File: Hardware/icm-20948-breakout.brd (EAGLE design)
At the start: 19.3 x 10.5 mm, 11 parts, among them J1 455-1750-1-ND, J2 455-1750-1-ND, U1 NCP563, U2 NTS0104, U3 ICM-20948

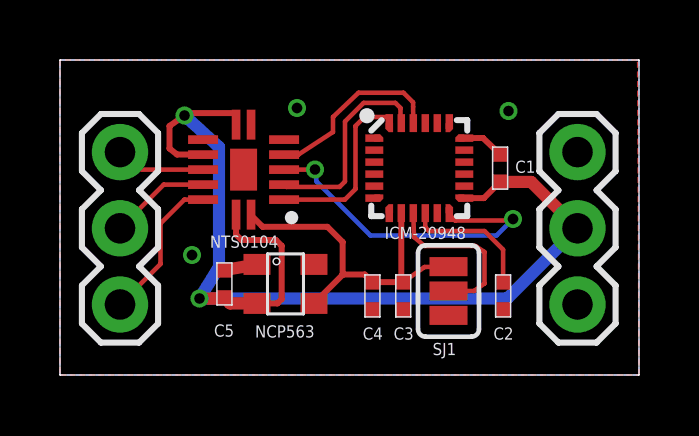
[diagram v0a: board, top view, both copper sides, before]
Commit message: Updated ICM footprint. The design rules of OSH Park are now met.
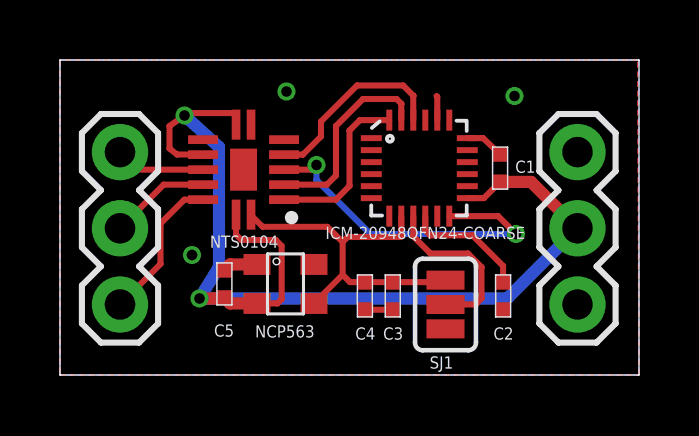
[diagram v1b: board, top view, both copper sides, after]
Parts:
- U3: value ICM-20948 -> ICM-20948QFN24-COARSE; device david-mems:QFN24-3X3 -> david-mems:SPARKFUN-SENSORS_MPU-9250
- moved SJ1 0.46 mm to (12.8, 2.35)
- moved C3 0.35 mm to (11.1, 2.64)
- moved C4 0.25 mm to (10.2, 2.64)
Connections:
- net GND: now also U3.20
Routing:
- net GND: track 2.59 -> 4.35 mm

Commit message: Fixed text layouts.
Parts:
- U3: value ICM-20948QFN24-COARSE -> ICM-20948
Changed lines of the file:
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@@
 <drawing>
 <settings>
-<setting alwaysvectorfont="no"/>
+<setting alwaysvectorfont="yes"/>
 <setting verticaltext="up"/>
 </settings>
@@
 <wire x1="0" y1="10.5" x2="0" y2="0" width="0" layer="20"/>
 <text x="6.5" y="1.25" size="0.4064" layer="21" font="vector" ratio="20">NCP563</text>
-<text x="4.2" y="7.25" size="0.4064" layer="22" ratio="20" rot="MR0">INT</text>
-<text x="4.2" y="4.65" size="0.4064" layer="22" ratio="20" rot="MR0">SCL</text>
-<text x="4.25" y="2.15" size="0.4064" layer="22" ratio="20" rot="MR0">SDA</text>
-<text x="16.1" y="4.3" size="0.4064" layer="22" ratio="20" rot="MR0">VCC</text>
-<text x="16.1" y="2.05" size="0.4064" layer="22" ratio="20" rot="MR0">GND</text>
+<text x="4.2" y="7.25" size="0.4064" layer="22" font="vector" ratio="20" rot="MR0">INT</text>
+<text x="4.2" y="4.65" size="0.4064" layer="22" font="vector" ratio="20" rot="MR0">SCL</text>
+<text x="4.25" y="2.15" size="0.4064" layer="22" font="vector" ratio="20" rot="MR0">SDA</text>
+<text x="16.25" y="5.1" size="0.4064" layer="22" font="vector" ratio="20" rot="MR0">VCC</text>
+<text x="16.2" y="2.15" size="0.4064" layer="22" font="vector" ratio="20" rot="MR0">GND</text>
 </plain>
 <attributes>
@@
 </autorouter>
 <elements>
-<element name="U3" library="david-mems" package="SPARKFUN-SENSORS_MPU-9250" value="ICM-20948QFN24-COARSE" x="11.976" y="6.896" smashed="yes">
-<attribute name="VALUE" x="12.176" y="4.941" size="0.4064" layer="21" ratio="20" align="top-center"/>
+<element name="U3" library="david-mems" package="SPARKFUN-SENSORS_MPU-9250" value="ICM-20948" x="11.976" y="6.896" smashed="yes">
+<attribute name="VALUE" x="11.976" y="4.791" size="0.4064" layer="21" font="vector" ratio="20" align="top-center"/>
 </element>
 <element name="U2" library="david-mems" package="SOT762-1" value="NTS0104" x="6.119" y="6.846" smashed="yes" rot="R90">
@@
 </element>
 <element name="SJ1" library="SparkFun-Passives" package="SJ_3_PASTE2&amp;3" value="JUMPER-32-3" x="12.85" y="2.35" smashed="yes" rot="R270">
-<attribute name="NAME" x="12.32" y="0.213" size="0.4064" layer="25" ratio="10"/>
+<attribute name="NAME" x="12.32" y="0.213" size="0.4064" layer="25" font="vector" ratio="20"/>
 <attribute name="VALUE" x="12.85" y="2.4501" size="0.02" layer="27"/>
 </element>
